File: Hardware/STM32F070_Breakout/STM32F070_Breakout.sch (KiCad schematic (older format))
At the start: 37 parts, among them J1 10118194-0001LF, J2 Conn_01x16, J3 Conn_01x16, J4 Conn_01x05, J5 Conn_01x01, J6 Conn_01x01, J7 Conn_01x01, SW1 SW_Push, SW2 SW_Push, U1 AP2112K-3.3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

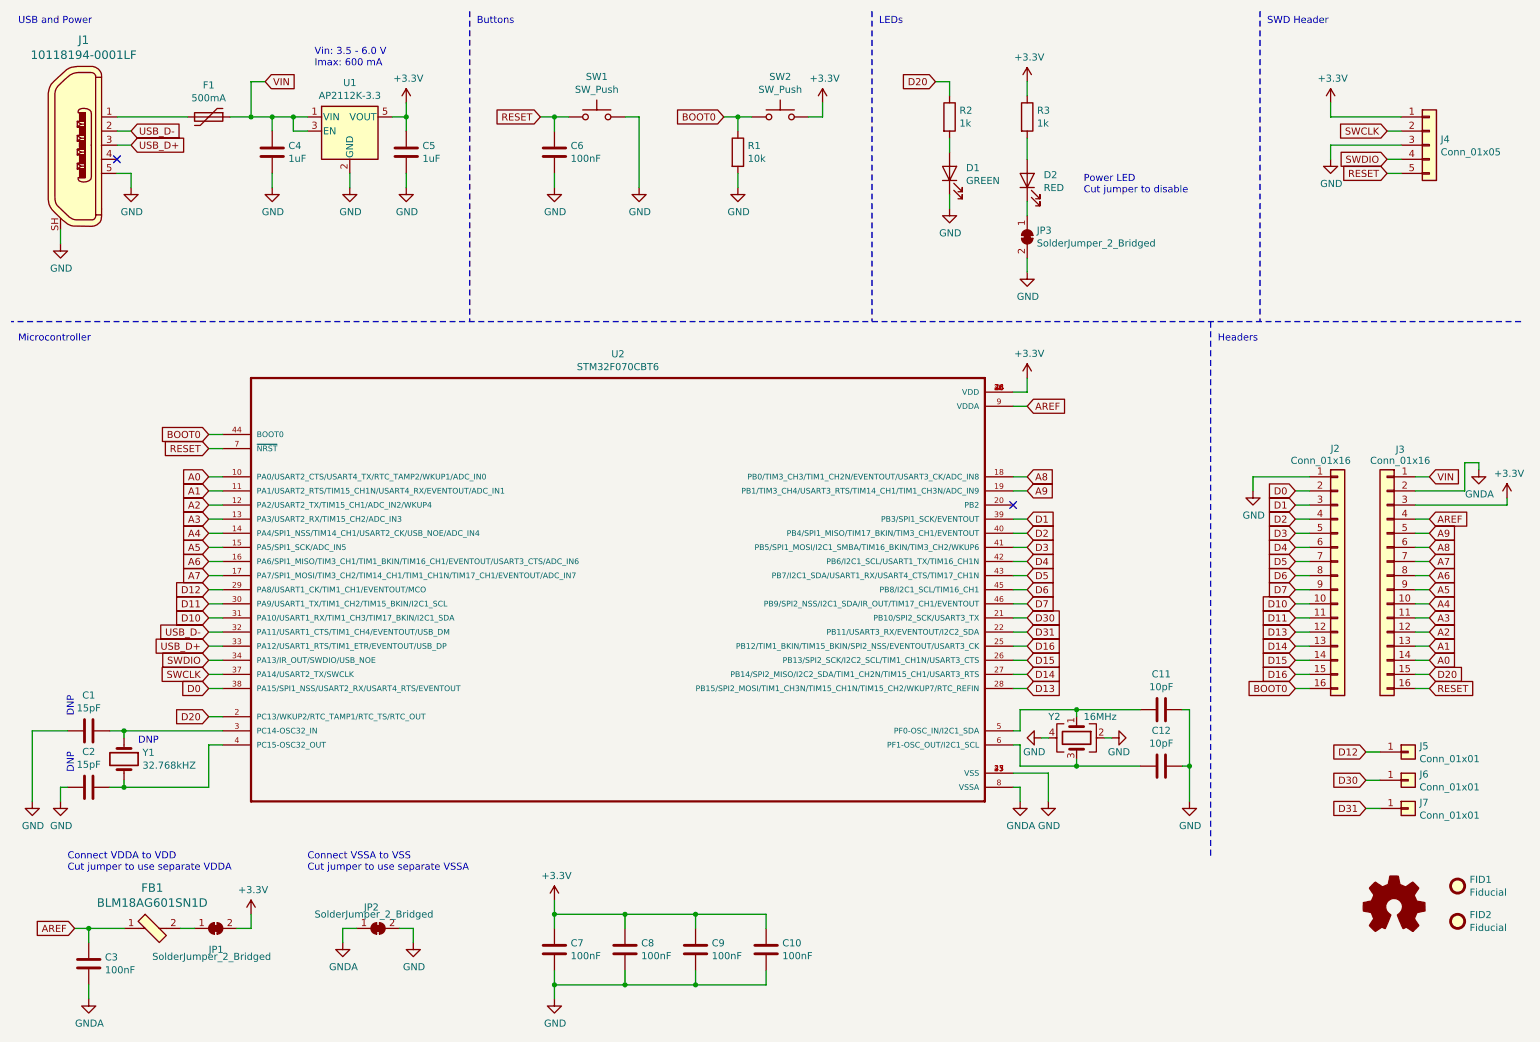
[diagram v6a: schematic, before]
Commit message: Added schematic pdf
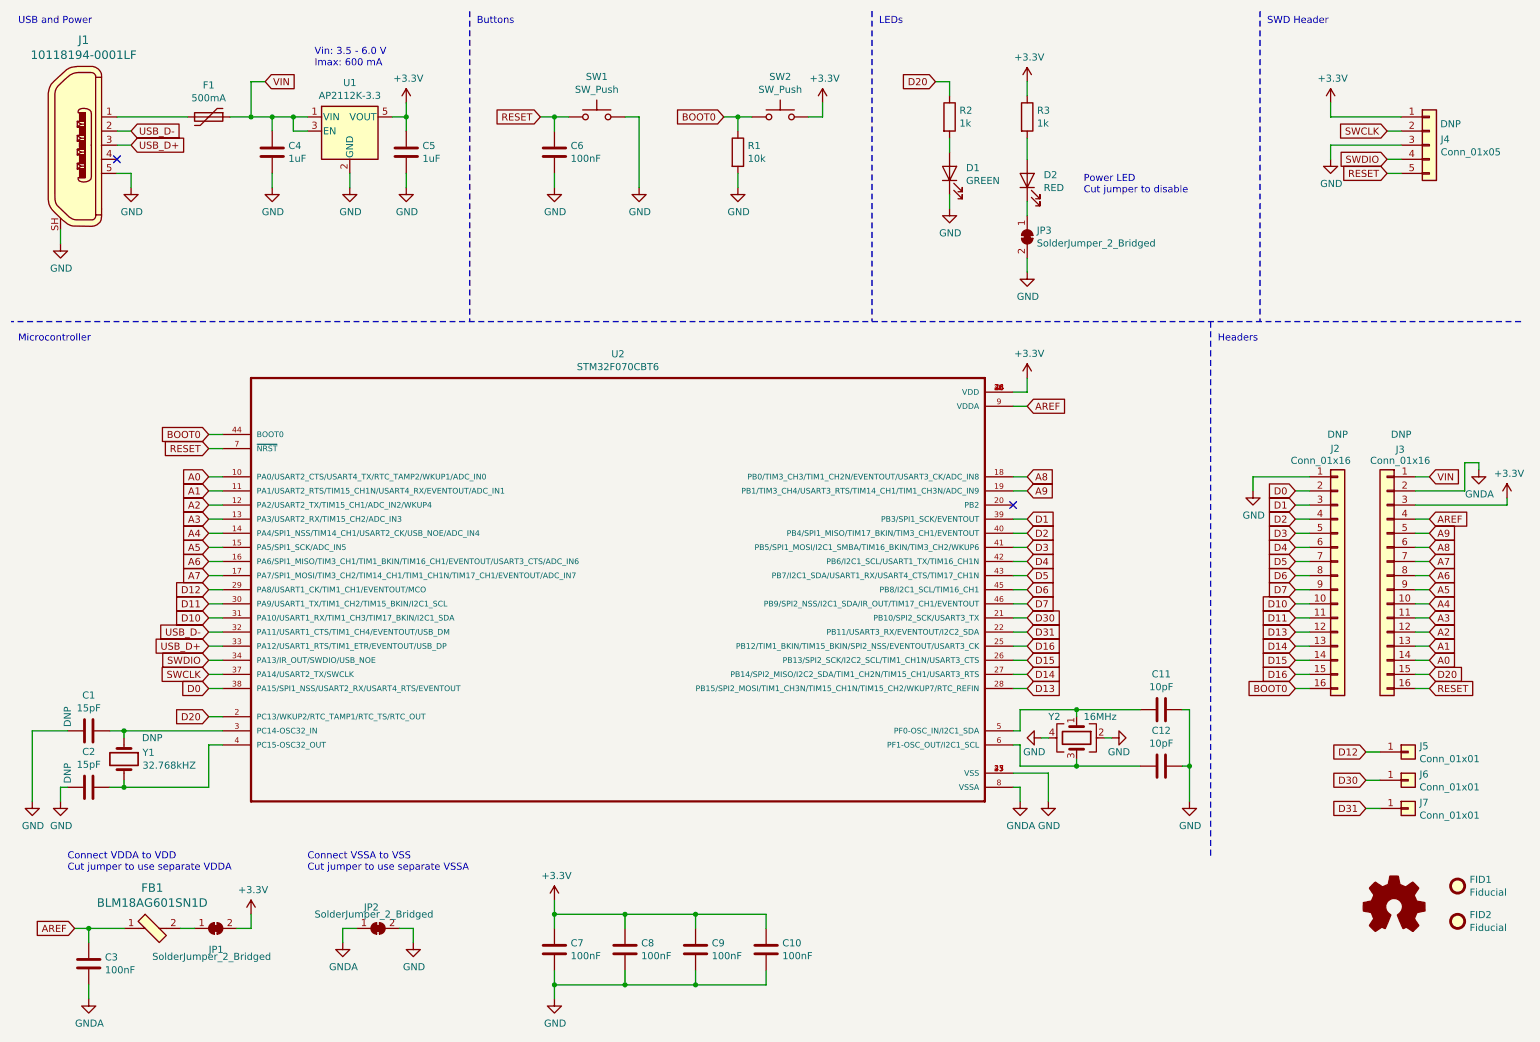
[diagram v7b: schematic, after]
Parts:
- C1, C2, J2, J3, J4, Y1: Config (none) -> DNP
- J1: footprint digikey-footprints:USB_Micro_B_Female_10118194-0001LF -> STM32F070_Breakout:USB_Micro_B_Female_10118194-0001LF_oversized_pads
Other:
- note removed: "DNP"
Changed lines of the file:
@@
 Text Notes 8100 1800 0    50   ~ 0
 Power LED\nCut jumper to disable
-$Comp
-L STM32F070CBT6:STM32F070CBT6 U2
-U 1 1 5CF0F9EF
-P 4800 4600
-F 0 "U2" H 4800 6270 50  0000 C CNN
-F 1 "STM32F070CBT6" H 4800 6179 50  0000 C CNN
-F 2 "STM32F070CBT6:QFP50P900X900X160-48N" H 4800 4600 50  0001 L BNN
-F 3 "" H 4800 4600 50  0001 L BNN
-F 4 "Entry-level ARM Cortex-M0 Value line MCU with up to 128 Kbytes Flash, 48 MHz CPU" H 4800 4600 50  0001 L BNN "Field4"
-F 5 "STMicroelectronics" H 4800 4600 50  0001 L BNN "Field5"
-F 6 "None" H 4800 4600 50  0001 L BNN "Field6"
-F 7 "STM32F070CBT6" H 4800 4600 50  0001 L BNN "Field7"
-F 8 "LQFP-48 STMicroelectronics" H 4800 4600 50  0001 L BNN "Field8"
-	1    4800 4600
-	1    0    0    -1
-$EndComp
 Text GLabel 1350 1450 2    50   Input ~ 0
 USB_D+
@@
 F 2 "STM32F070_Breakout:PinHeader_1x05_P2.54mm_Vertical_NoSilk" H 10550 1450 50  0001 C CNN
 F 3 "~" H 10550 1450 50  0001 C CNN
+F 4 "DNP" H 10700 1600 50  0000 C CNN "Config"
 	1    10550 1450
 	1    0    0    -1
@@
 Wire Wire Line
 	4850 7300 4850 7400
-Wire Wire Line
-	4850 7400 4350 7400
 Connection ~ 4350 7400
 Wire Wire Line
@@
 Wire Wire Line
 	5350 7300 5350 7400
-Wire Wire Line
-	5350 7400 4850 7400
 Connection ~ 4850 7400
 Wire Wire Line
 	5850 7300 5850 7400
-Wire Wire Line
-	5850 7400 5350 7400
 Connection ~ 5350 7400
 Text GLabel 7700 3800 2    50   Input ~ 0
@@
 F 2 "Crystal:Crystal_SMD_G8-2Pin_3.2x1.5mm" H 1300 5800 50  0001 C CNN
 F 3 "~" H 1300 5800 50  0001 C CNN
+F 4 "DNP" V 1150 6000 50  0000 C CNN "Config"
 	1    1300 5800
-	0    1    1    0
-$EndComp
-$Comp
-L Device:C C2
-U 1 1 5D187B26
-P 1050 6000
-F 0 "C2" V 798 6000 50  0000 C CNN
-F 1 "15pF" V 889 6000 50  0000 C CNN
-F 2 "Capacitor_SMD:C_0603_1608Metric" H 1088 5850 50  0001 C CNN
-F 3 "~" H 1050 6000 50  0001 C CNN
-	1    1050 6000
 	0    1    1    0
 $EndComp
@@
 F 2 "Capacitor_SMD:C_0603_1608Metric" H 1088 5450 50  0001 C CNN
 F 3 "~" H 1050 5600 50  0001 C CNN
+F 4 "DNP" H 950 5450 50  0000 C CNN "Config"
 	1    1050 5600
 	0    1    1    0
@@
 Wire Wire Line
 	7650 5700 7650 5850
-Text Notes 1400 5700 0    50   ~ 0
-DNP
-Text Notes 950  5500 1    50   ~ 0
-DNP
-Text Notes 950  5900 1    50   ~ 0
-DNP
 Wire Notes Line
 	11200 2700 500  2700
@@
 F 2 "STM32F070_Breakout:PinHeader_1x16_P2.54mm_Vertical_NoSilk" H 9900 4500 50  0001 C CNN
 F 3 "~" H 9900 4500 50  0001 C CNN
+F 4 "DNP" H 9900 5500 50  0000 C CNN "Config"
 	1    9900 4500
 	1    0    0    -1
@@
 F 2 "STM32F070_Breakout:PinHeader_1x16_P2.54mm_Vertical_NoSilk" H 10250 4500 50  0001 C CNN
 F 3 "~" H 10250 4500 50  0001 C CNN
+F 4 "DNP" H 10150 5500 50  0000 C CNN "Config"
 	1    10250 4500
 	-1   0    0    -1
@@
 F 0 "J1" H 1014 2195 60  0000 C CNN
 F 1 "10118194-0001LF" H 1014 2089 60  0000 C CNN
-F 2 "digikey-footprints:USB_Micro_B_Female_10118194-0001LF" H 1150 1650 60  0001 L CNN
+F 2 "STM32F070_Breakout:USB_Micro_B_Female_10118194-0001LF_oversized_pads" H 1150 1650 60  0001 L CNN
 F 3 "http://www.amphenol-icc.com/media/wysiwyg/files/drawing/10118194.pdf" H 1150 1750 60  0001 L CNN
 F 4 "609-4618-1-ND" H 1150 1850 60  0001 L CNN "Digi-Key_PN"
@@
 Text GLabel 7700 4800 2    50   Input ~ 0
 D30
+Wire Wire Line
+	5350 7400 4850 7400
+Wire Wire Line
+	4850 7400 4350 7400
+Wire Wire Line
+	5850 7400 5350 7400
+$Comp
+L STM32F070CBT6:STM32F070CBT6 U2
+U 1 1 5CF0F9EF
+P 4800 4600
+F 0 "U2" H 4800 6270 50  0000 C CNN
+F 1 "STM32F070CBT6" H 4800 6179 50  0000 C CNN
+F 2 "STM32F070CBT6:QFP50P900X900X160-48N" H 4800 4600 50  0001 L BNN
+F 3 "" H 4800 4600 50  0001 L BNN
+F 4 "Entry-level ARM Cortex-M0 Value line MCU with up to 128 Kbytes Flash, 48 MHz CPU" H 4800 4600 50  0001 L BNN "Field4"
+F 5 "STMicroelectronics" H 4800 4600 50  0001 L BNN "Field5"
+F 6 "None" H 4800 4600 50  0001 L BNN "Field6"
+F 7 "STM32F070CBT6" H 4800 4600 50  0001 L BNN "Field7"
+F 8 "LQFP-48 STMicroelectronics" H 4800 4600 50  0001 L BNN "Field8"
+	1    4800 4600
+	1    0    0    -1
+$EndComp
+$Comp
+L Device:C C2
+U 1 1 5D187B26
+P 1050 6000
+F 0 "C2" V 798 6000 50  0000 C CNN
+F 1 "15pF" V 889 6000 50  0000 C CNN
+F 2 "Capacitor_SMD:C_0603_1608Metric" H 1088 5850 50  0001 C CNN
+F 3 "~" H 1050 6000 50  0001 C CNN
+F 4 "DNP" H 950 5850 50  0000 C CNN "Config"
+	1    1050 6000
+	0    1    1    0
+$EndComp
 $EndSCHEMATC
